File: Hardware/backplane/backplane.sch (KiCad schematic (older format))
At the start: 45 parts, among them J1 USB_B_Micro, SW1 SW_SPST, U2 MAX811SEUS-T, U3 MAX811SEUS-T, U4 PAL24, X1 CXO_DIP8

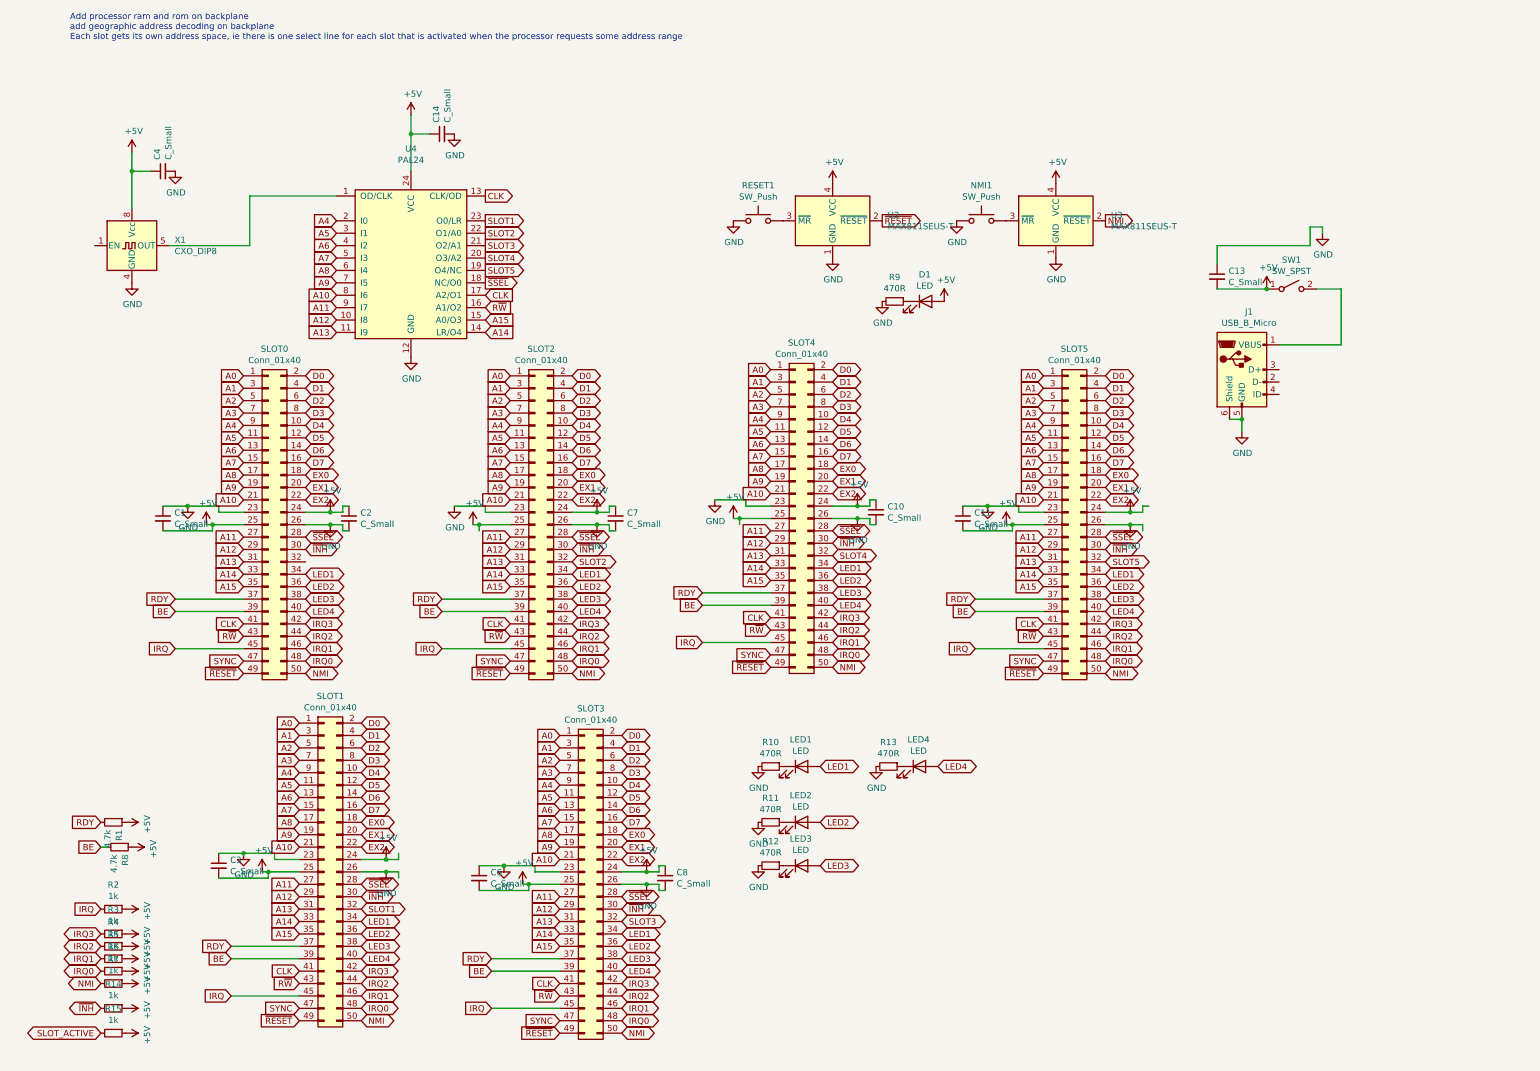
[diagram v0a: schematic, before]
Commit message: Clean up schematics and add pdfs
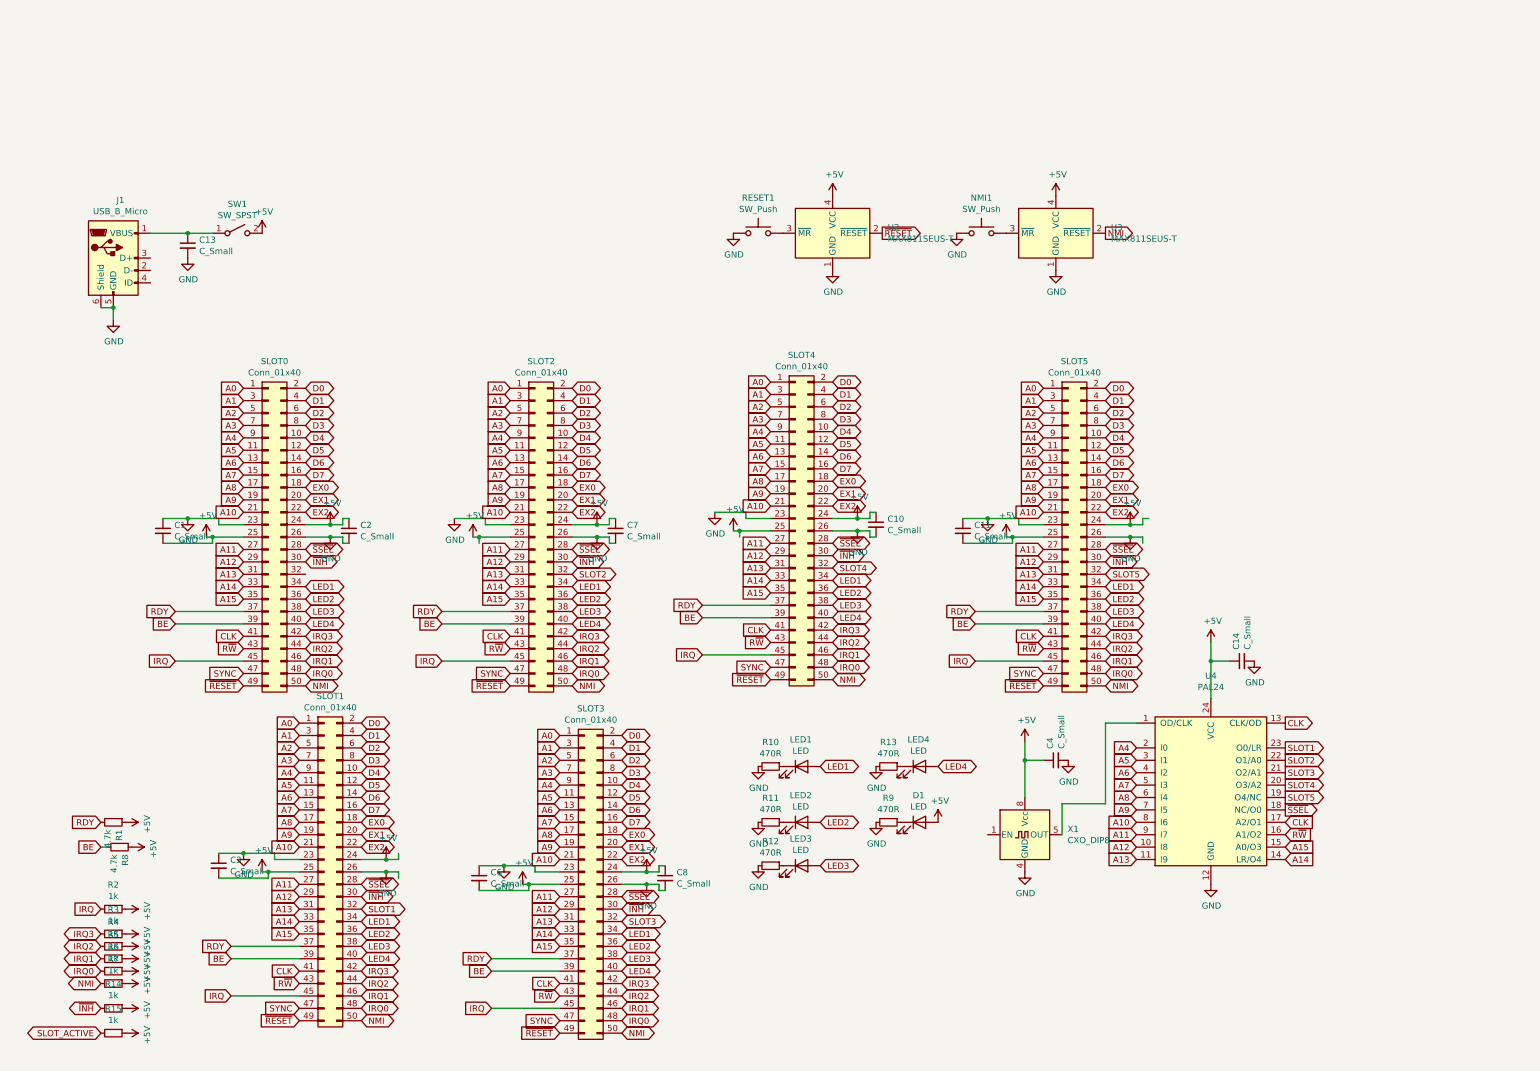
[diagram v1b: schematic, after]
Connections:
- wire segments 128 -> 122
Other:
- note removed: "Add processor ram and rom on backplane\nadd geographic address decoding on backplane\nEach slot gets its own address space, ie there is one select line for each slot that is activated when the processor requests some address range"
- moved on the sheet: C1, C10, C11, C13, C14, C2, C4, C7, D1, J1, NMI1, R9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

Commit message: Each slot has an individual interrupt line, to prevent two cards using the same interrupt line.
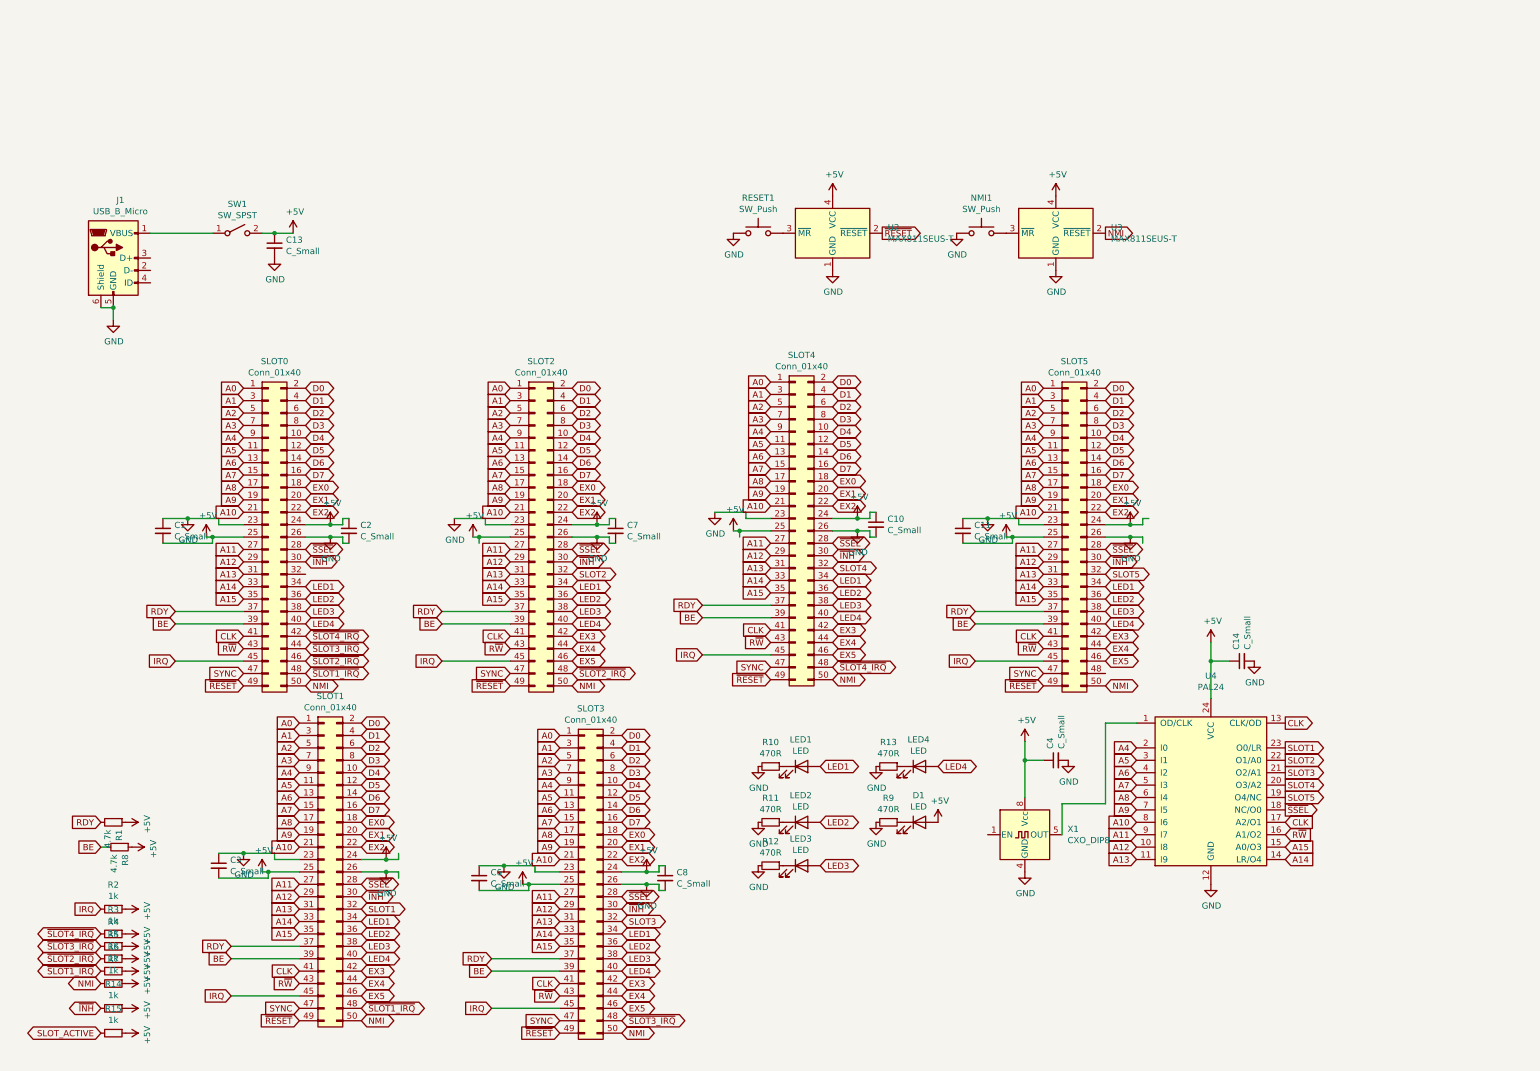
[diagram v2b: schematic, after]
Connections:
- net labels added: EX3, EX4, EX5, ~SLOT1_IRQ~, ~SLOT2_IRQ~, ~SLOT3_IRQ~, ~SLOT4_IRQ~
- net labels removed: IRQ0, IRQ1, IRQ2, IRQ3
- wire segments 122 -> 123
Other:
- moved on the sheet: C13
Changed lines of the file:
@@
 Text GLabel 1750 4550 0    50   Input ~ 0
 IRQ
-Text GLabel 2800 4650 2    50   BiDi ~ 0
-IRQ0
-Text GLabel 2800 4550 2    50   BiDi ~ 0
-IRQ1
-Text GLabel 2800 4450 2    50   BiDi ~ 0
-IRQ2
-Text GLabel 2800 4350 2    50   BiDi ~ 0
-IRQ3
 $Comp
 L Device:C_Small C2
@@
 Text GLabel 1150 7150 0    50   BiDi ~ 0
 NMI
+Text GLabel 1150 6750 0    50   BiDi ~ 0
+~SLOT4_IRQ~
+Text GLabel 1150 6850 0    50   BiDi ~ 0
+~SLOT3_IRQ~
+Text GLabel 1150 6950 0    50   BiDi ~ 0
+~SLOT2_IRQ~
 Text GLabel 1150 7050 0    50   BiDi ~ 0
-IRQ0
-Text GLabel 1150 6950 0    50   BiDi ~ 0
-IRQ1
-Text GLabel 1150 6850 0    50   BiDi ~ 0
-IRQ2
-Text GLabel 1150 6750 0    50   BiDi ~ 0
-IRQ3
+~SLOT1_IRQ~
 Text GLabel 1150 6550 0    50   Input ~ 0
 IRQ
@@
 IRQ
 Text GLabel 4950 4650 2    50   BiDi ~ 0
-IRQ0
-Text GLabel 4950 4550 2    50   BiDi ~ 0
-IRQ1
-Text GLabel 4950 4450 2    50   BiDi ~ 0
-IRQ2
-Text GLabel 4950 4350 2    50   BiDi ~ 0
-IRQ3
+~SLOT2_IRQ~
 $Comp
 L Device:C_Small C7
@@
 IRQ
 Text GLabel 7050 4600 2    50   BiDi ~ 0
-IRQ0
-Text GLabel 7050 4500 2    50   BiDi ~ 0
-IRQ1
-Text GLabel 7050 4400 2    50   BiDi ~ 0
-IRQ2
-Text GLabel 7050 4300 2    50   BiDi ~ 0
-IRQ3
+~SLOT4_IRQ~
 $Comp
 L Device:C_Small C10
@@
 Text GLabel 8200 4550 0    50   Input ~ 0
 IRQ
-Text GLabel 9250 4650 2    50   BiDi ~ 0
-IRQ0
-Text GLabel 9250 4550 2    50   BiDi ~ 0
-IRQ1
-Text GLabel 9250 4450 2    50   BiDi ~ 0
-IRQ2
-Text GLabel 9250 4350 2    50   BiDi ~ 0
-IRQ3
 Wire Wire Line
 	9600 3400 9550 3400
@@
 IRQ
 Text GLabel 3250 7350 2    50   BiDi ~ 0
-IRQ0
-Text GLabel 3250 7250 2    50   BiDi ~ 0
-IRQ1
-Text GLabel 3250 7150 2    50   BiDi ~ 0
-IRQ2
-Text GLabel 3250 7050 2    50   BiDi ~ 0
-IRQ3
+~SLOT1_IRQ~
 Wire Wire Line
 	3550 6100 3550 6150
@@
 IRQ
 Text GLabel 5350 7450 2    50   BiDi ~ 0
-IRQ0
-Text GLabel 5350 7350 2    50   BiDi ~ 0
-IRQ1
-Text GLabel 5350 7250 2    50   BiDi ~ 0
-IRQ2
-Text GLabel 5350 7150 2    50   BiDi ~ 0
-IRQ3
+~SLOT3_IRQ~
 $Comp
 L Device:C_Small C8
@@
 L power:GND #PWR0133
 U 1 1 60033398
-P 1850 1300
-F 0 "#PWR0133" H 1850 1050 50  0001 C CNN
-F 1 "GND" H 1855 1127 50  0000 C CNN
-F 2 "" H 1850 1300 50  0001 C CNN
-F 3 "" H 1850 1300 50  0001 C CNN
-	1    1850 1300
+P 2550 1300
+F 0 "#PWR0133" H 2550 1050 50  0001 C CNN
+F 1 "GND" H 2555 1127 50  0000 C CNN
+F 2 "" H 2550 1300 50  0001 C CNN
+F 3 "" H 2550 1300 50  0001 C CNN
+	1    2550 1300
 	1    0    0    -1
 $EndComp
@@
 L power:+5V #PWR0134
 U 1 1 60039848
-P 2450 1100
-F 0 "#PWR0134" H 2450 950 50  0001 C CNN
-F 1 "+5V" H 2465 1273 50  0000 C CNN
-F 2 "" H 2450 1100 50  0001 C CNN
-F 3 "" H 2450 1100 50  0001 C CNN
-	1    2450 1100
+P 2700 1100
+F 0 "#PWR0134" H 2700 950 50  0001 C CNN
+F 1 "+5V" H 2715 1273 50  0000 C CNN
+F 2 "" H 2700 1100 50  0001 C CNN
+F 3 "" H 2700 1100 50  0001 C CNN
+	1    2700 1100
 	1    0    0    -1
 $EndComp
@@
 L Device:C_Small C13
 U 1 1 6003A557
-P 1850 1200
-F 0 "C13" H 1942 1246 50  0000 L CNN
-F 1 "C_Small" H 1942 1155 50  0000 L CNN
-F 2 "Capacitor_THT:CP_Radial_D6.3mm_P2.50mm" H 1850 1200 50  0001 C CNN
-F 3 "~" H 1850 1200 50  0001 C CNN
-	1    1850 1200
+P 2550 1200
+F 0 "C13" H 2642 1246 50  0000 L CNN
+F 1 "C_Small" H 2642 1155 50  0000 L CNN
+F 2 "Capacitor_THT:CP_Radial_D6.3mm_P2.50mm" H 2550 1200 50  0001 C CNN
+F 3 "~" H 2550 1200 50  0001 C CNN
+	1    2550 1200
 	1    0    0    -1
 $EndComp
@@
 	1    0    0    -1
 $EndComp
-Wire Wire Line
-	2050 1100 1850 1100
 $Comp
 L Connector:USB_B_Micro J1
@@
 Wire Wire Line
 	9250 5050 9500 5050
-Connection ~ 1850 1100
-Wire Wire Line
-	1850 1100 1550 1100
 Connection ~ 1250 1700
+Text GLabel 4950 4350 2    50   BiDi ~ 0
+EX3
+Text GLabel 4950 4450 2    50   BiDi ~ 0
+EX4
+Text GLabel 4950 4550 2    50   BiDi ~ 0
+EX5
+Text GLabel 7050 4300 2    50   BiDi ~ 0
+EX3
+Text GLabel 7050 4400 2    50   BiDi ~ 0
+EX4
+Text GLabel 7050 4500 2    50   BiDi ~ 0
+EX5
+Text GLabel 9250 4350 2    50   BiDi ~ 0
+EX3
+Text GLabel 9250 4450 2    50   BiDi ~ 0
+EX4
+Text GLabel 9250 4550 2    50   BiDi ~ 0
+EX5
+Text GLabel 5350 7150 2    50   BiDi ~ 0
+EX3
+Text GLabel 5350 7250 2    50   BiDi ~ 0
+EX4
+Text GLabel 5350 7350 2    50   BiDi ~ 0
+EX5
+Text GLabel 3250 7050 2    50   BiDi ~ 0
+EX3
+Text GLabel 3250 7150 2    50   BiDi ~ 0
+EX4
+Text GLabel 3250 7250 2    50   BiDi ~ 0
+EX5
+Text GLabel 2800 4350 2    50   BiDi ~ 0
+~SLOT4_IRQ~
+Text GLabel 2800 4450 2    50   BiDi ~ 0
+~SLOT3_IRQ~
+Text GLabel 2800 4550 2    50   BiDi ~ 0
+~SLOT2_IRQ~
+Text GLabel 2800 4650 2    50   BiDi ~ 0
+~SLOT1_IRQ~
+Wire Wire Line
+	2700 1100 2550 1100
+Connection ~ 2550 1100
+Wire Wire Line
+	2550 1100 2450 1100
+Wire Wire Line
+	1550 1100 2050 1100
 $EndSCHEMATC

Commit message: Update pin names
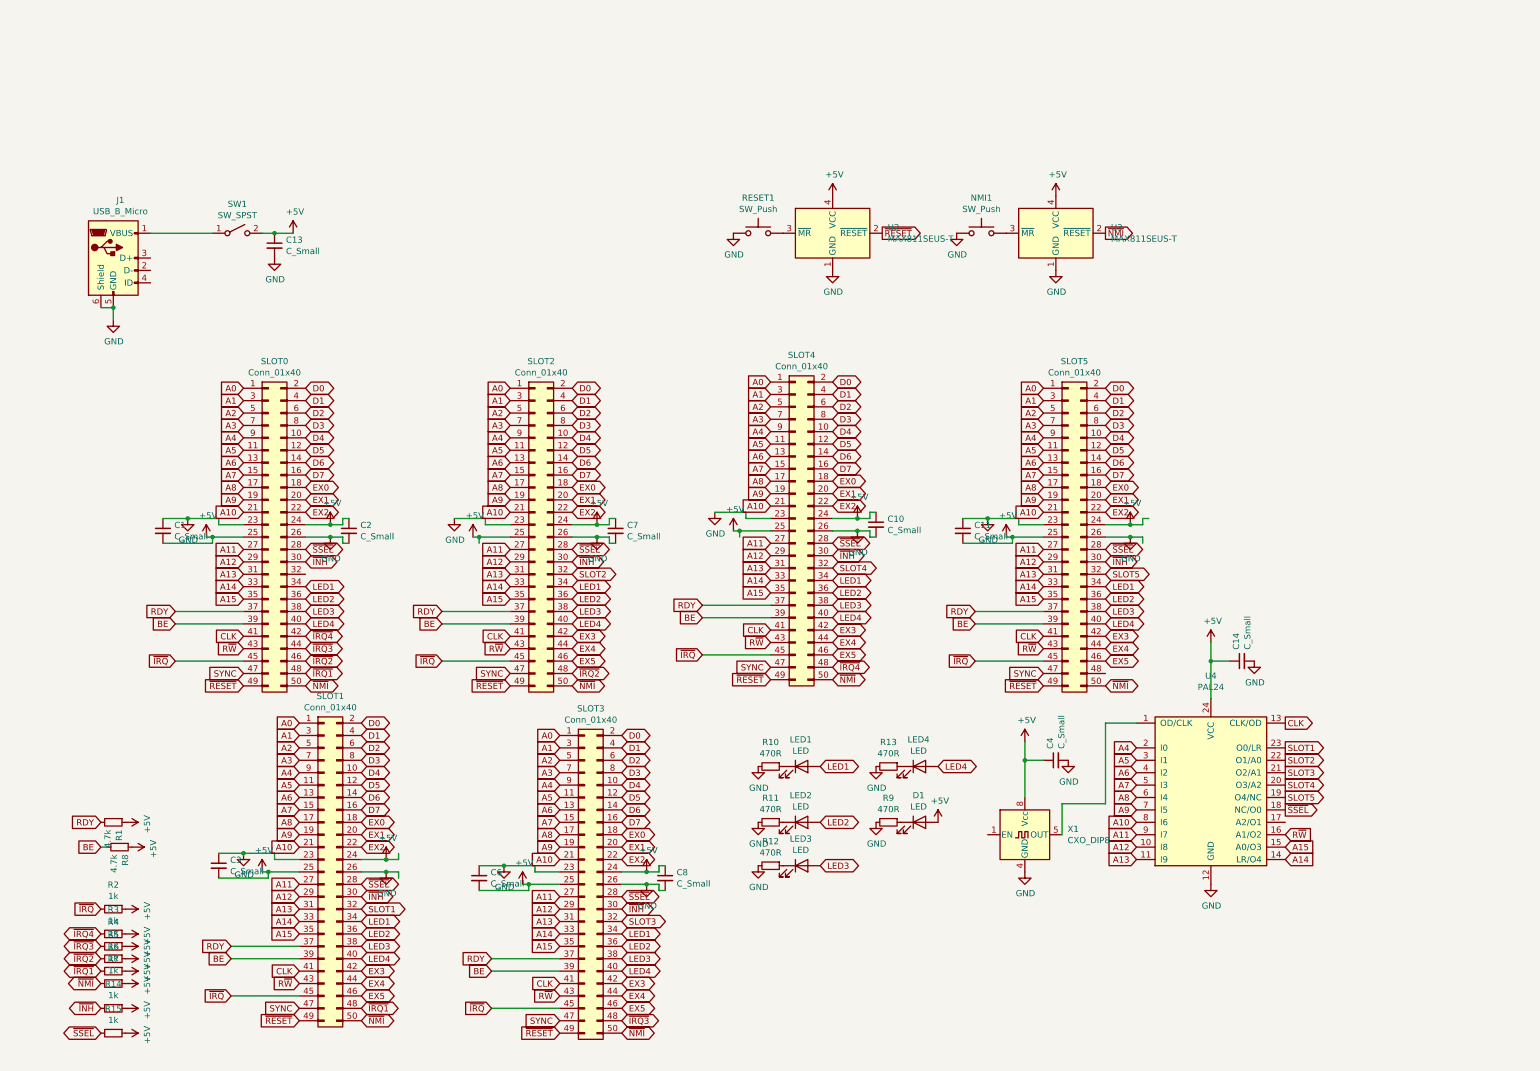
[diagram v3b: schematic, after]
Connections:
- net labels added: ~IRQ1~, ~IRQ2~, ~IRQ3~, ~IRQ4~, ~IRQ~, ~NMI~
- net labels removed: IRQ, NMI, SLOT_ACTIVE, ~SLOT1_IRQ~, ~SLOT2_IRQ~, ~SLOT3_IRQ~, ~SLOT4_IRQ~
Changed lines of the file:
@@
 ~RESET~
 Text GLabel 2800 4750 2    50   BiDi ~ 0
-NMI
+~NMI~
 Text GLabel 1750 4150 0    50   Input ~ 0
 RDY
@@
 SYNC
 Text GLabel 1750 4550 0    50   Input ~ 0
-IRQ
+~IRQ~
 $Comp
 L Device:C_Small C2
@@
 	2050 3550 2000 3550
 Text GLabel 1150 7150 0    50   BiDi ~ 0
-NMI
+~NMI~
 Text GLabel 1150 6750 0    50   BiDi ~ 0
-~SLOT4_IRQ~
+~IRQ4~
 Text GLabel 1150 6850 0    50   BiDi ~ 0
-~SLOT3_IRQ~
+~IRQ3~
 Text GLabel 1150 6950 0    50   BiDi ~ 0
-~SLOT2_IRQ~
+~IRQ2~
 Text GLabel 1150 7050 0    50   BiDi ~ 0
-~SLOT1_IRQ~
+~IRQ1~
 Text GLabel 1150 6550 0    50   Input ~ 0
-IRQ
+~IRQ~
 Text GLabel 1150 5850 0    50   Input ~ 0
 RDY
@@
 ~RESET~
 Text GLabel 4950 4750 2    50   BiDi ~ 0
-NMI
+~NMI~
 Text GLabel 3900 4150 0    50   Input ~ 0
 RDY
@@
 SYNC
 Text GLabel 3900 4550 0    50   Input ~ 0
-IRQ
+~IRQ~
 Text GLabel 4950 4650 2    50   BiDi ~ 0
-~SLOT2_IRQ~
+~IRQ2~
 $Comp
 L Device:C_Small C7
@@
 ~RESET~
 Text GLabel 7050 4700 2    50   BiDi ~ 0
-NMI
+~NMI~
 Text GLabel 6000 4100 0    50   Input ~ 0
 RDY
@@
 SYNC
 Text GLabel 6000 4500 0    50   Input ~ 0
-IRQ
+~IRQ~
 Text GLabel 7050 4600 2    50   BiDi ~ 0
-~SLOT4_IRQ~
+~IRQ4~
 $Comp
 L Device:C_Small C10
@@
 ~RESET~
 Text GLabel 9250 4750 2    50   BiDi ~ 0
-NMI
+~NMI~
 Text GLabel 8200 4150 0    50   Input ~ 0
 RDY
@@
 SYNC
 Text GLabel 8200 4550 0    50   Input ~ 0
-IRQ
+~IRQ~
 Wire Wire Line
 	9600 3400 9550 3400
@@
 ~RESET~
 Text GLabel 3250 7450 2    50   BiDi ~ 0
-NMI
+~NMI~
 Text GLabel 2200 6850 0    50   Input ~ 0
 RDY
@@
 SYNC
 Text GLabel 2200 7250 0    50   Input ~ 0
-IRQ
+~IRQ~
 Text GLabel 3250 7350 2    50   BiDi ~ 0
-~SLOT1_IRQ~
+~IRQ1~
 Wire Wire Line
 	3550 6100 3550 6150
@@
 ~RESET~
 Text GLabel 5350 7550 2    50   BiDi ~ 0
-NMI
+~NMI~
 Text GLabel 4300 6950 0    50   Input ~ 0
 RDY
@@
 SYNC
 Text GLabel 4300 7350 0    50   Input ~ 0
-IRQ
+~IRQ~
 Text GLabel 5350 7450 2    50   BiDi ~ 0
-~SLOT3_IRQ~
+~IRQ3~
 $Comp
 L Device:C_Small C8
@@
 $EndComp
 Text GLabel 9250 1100 2    50   Output ~ 0
-NMI
+~NMI~
 Text GLabel 7450 1100 2    50   Output ~ 0
 ~RESET~
@@
 Text GLabel 10700 6050 2    50   Input ~ 0
 A15
-Text GLabel 10700 5850 2    50   Input ~ 0
-CLK
 Text GLabel 10700 5950 2    50   Input ~ 0
 R~W~
@@
 $EndComp
 Text GLabel 1150 7550 0    50   BiDi ~ 0
-SLOT_ACTIVE
+~SSEL~
 $Comp
 L Device:R_Small R15
@@
 EX5
 Text GLabel 2800 4350 2    50   BiDi ~ 0
-~SLOT4_IRQ~
+~IRQ4~
 Text GLabel 2800 4450 2    50   BiDi ~ 0
-~SLOT3_IRQ~
+~IRQ3~
 Text GLabel 2800 4550 2    50   BiDi ~ 0
-~SLOT2_IRQ~
+~IRQ2~
 Text GLabel 2800 4650 2    50   BiDi ~ 0
-~SLOT1_IRQ~
+~IRQ1~
 Wire Wire Line
 	2700 1100 2550 1100
